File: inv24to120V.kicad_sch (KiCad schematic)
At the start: 133 parts, among them IC1 FSAM50SM60A, J1 Conn_02x13_Odd_Even_MountingP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, J10 Screw_Terminal_01x01, J11 Screw_Terminal_01x01, J12 Screw_Terminal_01x01, J2 Conn_02x13_Odd_Even_MountingP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, J3 Screw_Terminal_01x01, J4 Conn_02x05_Odd_Even_MountingP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, J5 Screw_Terminal_01x02, J6 Screw_Terminal_01x03, J7 Screw_Terminal_01x03, J8 Screw_Terminal_01x03, J9 Screw_Terminal_01x02, K1 J0971CS5VDC.45, Q1 IRFZ44NPBF, Q2 IRFZ44NPBF, Q3 2SC1815, Q4 2SC1815, Q5 2SA1015, Q6 2SA1015, Q7 2SC1815, U1 ESP32-DEVKITC-32D, U10 PC817, U2 LM2576HVT-5, U3 ACS712ELCTR30AT, U4 ACS712ELCTR30AT, U5 LM2576HVT-5, U6 ISO7340CDW, U7 ISO7340CDW, U8 AMC1300BDWVR, U9 PC817

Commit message: start rout
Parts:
- removed J1, J2: Conn_02x13_Odd_Even_MountingPin, Connector_IDC:IDC-Header_2x13_P2.54mm_Vertical, symbol Connector_Generic_MountingPin:Conn_02x13_Odd_Even_MountingPin
- removed J10, J11, J12, J3: Screw_Terminal_01x01, TerminalBlock_Wuerth:Wuerth_REDCUBE-THR_WP-THRBU_74650073_THR, symbol Connector:Screw_Terminal_01x01
- C10, C11, C12, C24, C25, C26, C27, C28, C29, C30, C31, C33, C34, C5, C6, C7, C8, C9: footprint Capacitor_SMD:C_0805_2012Metric -> Capacitor_SMD:C_0805_2012Metric_Pad1.18x1.45mm_HandSolder
- C13, C14, C15: footprint Capacitor_SMD:C_0805_2012Metric -> Capacitor_SMD:C_1206_3216Metric_Pad1.33x1.80mm_HandSolder
- R10, R22, R23, R24, R25, R26, R27, R28, R29, R30, R31, R32, R33, R34, R35, R36, R37, R7, R8, R9: footprint Resistor_SMD:R_0805_2012Metric -> Resistor_SMD:R_0805_2012Metric_Pad1.20x1.40mm_HandSolder
- R40, R44: footprint Resistor_THT:R_Axial_DIN0207_L6.3mm_D2.5mm_P10.16mm_Horizontal -> Resistor_SMD:R_0805_2012Metric_Pad1.20x1.40mm_HandSolder
- U1: footprint inv24VLib:MODULE_ESP32-DEVKITC-32D -> Connector_PinSocket_2.54mm:PinSocket_2x20_P2.54mm_Vertical
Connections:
- net FAULT_IPM2 is gone; now on net FAULT_IPM: R44.2, U10.4
- net GNDPWR1 is gone; now on net GNDPWR: R19.1, U8.3 (INN), X1.12, X1.13
- net I_Uphase2 is gone; now on net I_Uphase: R7.1, R9.2
- net I_Vphase2 is gone; now on net I_Vphase: R10.2, R8.1
- net TEMPERATURE_IPM2 is gone; now on net TEMPERATURE_IPM: BX6.1, C34.2, R40.2
- net UH2 is gone; now on an unnamed net: R29.1
- net UL2 is gone; now on an unnamed net: R32.1
- net VH2 is gone; now on an unnamed net: R30.1
- net VL2 is gone; now on an unnamed net: R33.1
- net VTH_IPM2 is gone; now on net VTH_IPM: IC1.24 (VTH)
- net WH2 is gone; now on an unnamed net: R31.1
- net WL2 is gone; now on an unnamed net: R34.1
- net +3.3V: now also U1.1 (3V3), U1.3 (EN); no longer U1.J2-1 (3V3), U1.J2-2 (EN)
- net +5V: now also U1.37 (EXT_5V); no longer U1.J2-19 (EXT_5V)
- net ANALOG_CMD: now also U1.11 (IO35); no longer U1.J2-6 (IO35)
- net DIGITAL_CMD: now also U1.16 (IO19); no longer U1.J3-8 (IO19)
- net FAULT_IPM: now also U1.4 (IO23); no longer U1.J3-2 (IO23)
- net GND: now also U1.14 (GND2), U1.2 (GND3), U1.27 (GND1); no longer U1.J2-14 (GND1), U1.J3-1 (GND3), U1.J3-7 (GND2)
- net GNDPWR: now also IC1.16 (COM(H))
- net I2C_SCL: now also U1.6 (IO22); no longer U1.J3-3 (IO22)
- net I2C_SDA: now also U1.12 (IO21); no longer U1.J3-6 (IO21)
- net I_Uphase: now also U1.5 (SENSOR_VP); no longer U1.J2-3 (SENSOR_VP)
- net I_Vphase: now also U1.7 (SENSOR_VN); no longer U1.J2-4 (SENSOR_VN)
- net PWM0_H: now also U1.29 (IO13); no longer U1.J2-15 (IO13)
- net PWM0_L: now also U1.25 (IO12); no longer U1.J2-13 (IO12)
- net PWM1_H: now also U1.23 (IO14); no longer U1.J2-12 (IO14)
- net PWM1_L: now also U1.21 (IO27); no longer U1.J2-11 (IO27)
- net PWM2_H: now also U1.19 (IO26); no longer U1.J2-10 (IO26)
- net PWM2_L: now also U1.17 (IO25); no longer U1.J2-9 (IO25)
- net RELAY_TRIP: now also U1.18 (IO18); no longer U1.J3-9 (IO18)
- net SCI_RXD: now also U1.24 (IO16); no longer U1.J3-12 (IO16)
- net SCI_TXD: now also U1.22 (IO17); no longer U1.J3-11 (IO17)
- net TEMPERATURE_IPM: now also U1.13 (IO32); no longer U1.J2-7 (IO32)
- net VBUS: now also L4.1, R17.2
- net VDC_sensor: now also U1.9 (IO34); no longer U1.J2-5 (IO34)
- net 150V_OUT1 renamed 150V_OUT
- net UH1: no longer names the net of U6.14 (OUTA)
- net UL1: no longer names the net of U7.14 (OUTA)
- net VH1: no longer names the net of U6.13 (OUTB)
- net VL1: no longer names the net of U7.13 (OUTB)
- net VTH_IPM1 renamed VTH_IPM
- net WH1: no longer names the net of U6.12 (OUTC)
- net WL1: no longer names the net of U7.12 (OUTC)
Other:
- moved on the sheet: C22

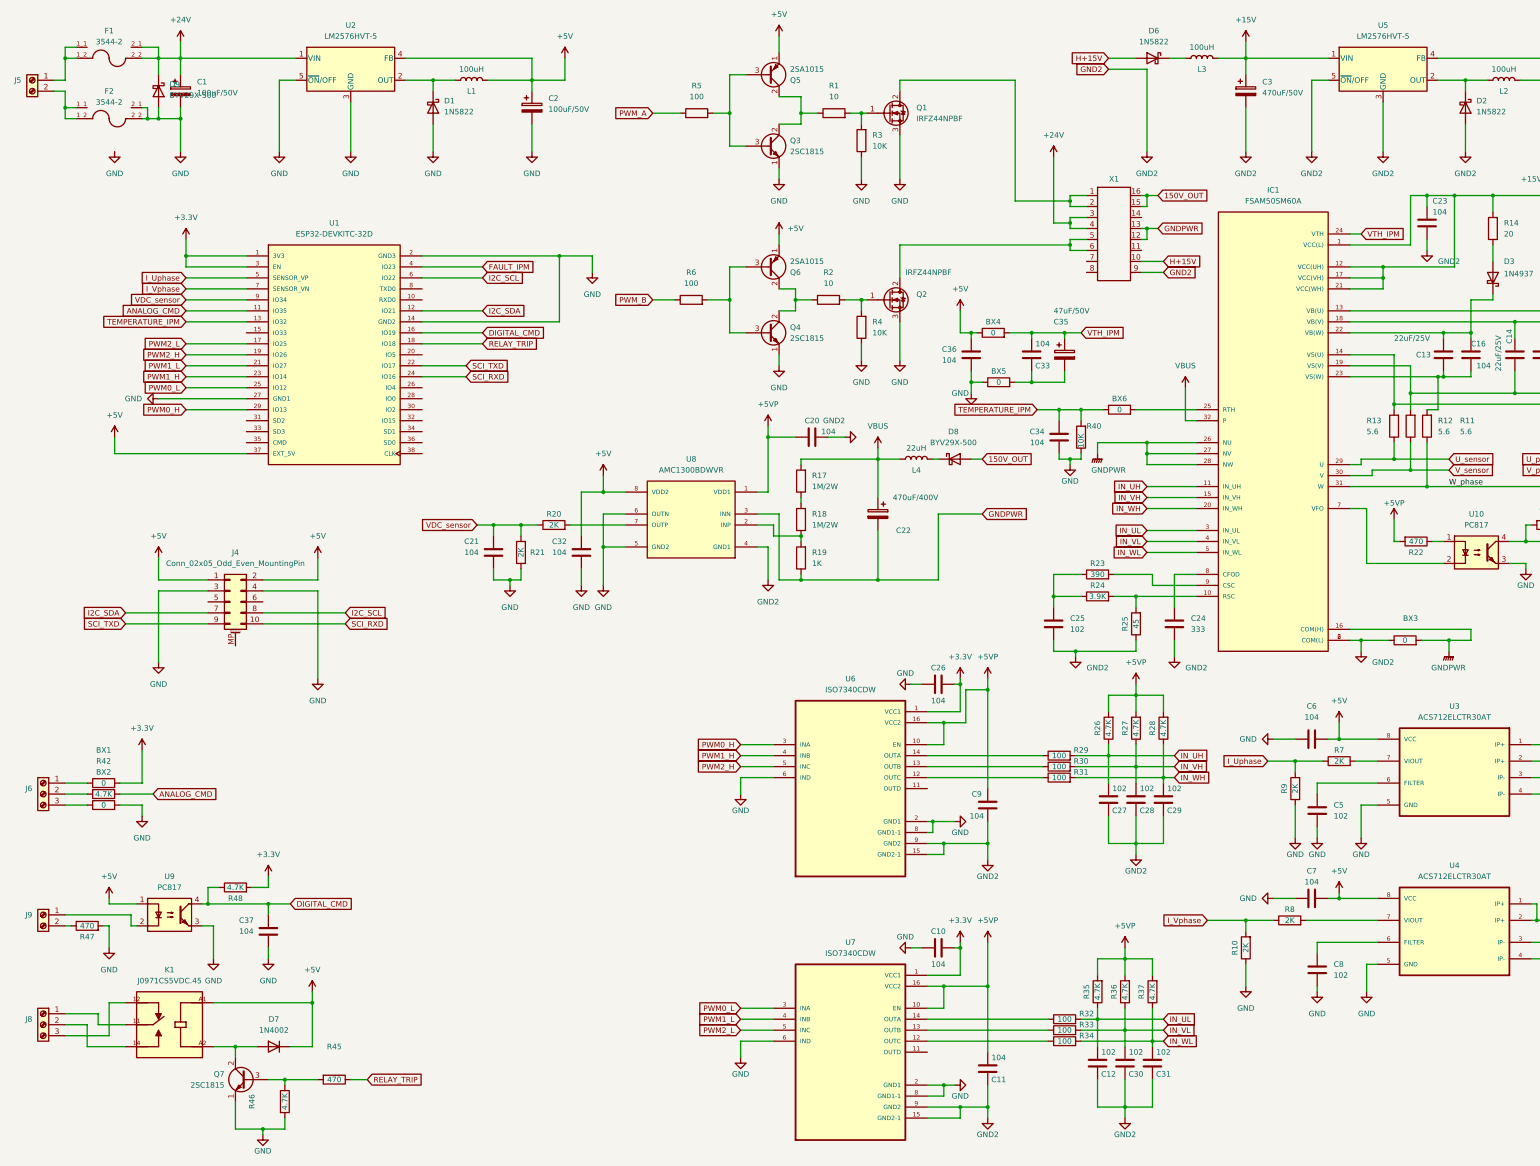
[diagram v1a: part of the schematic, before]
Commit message: remove aux addon connect
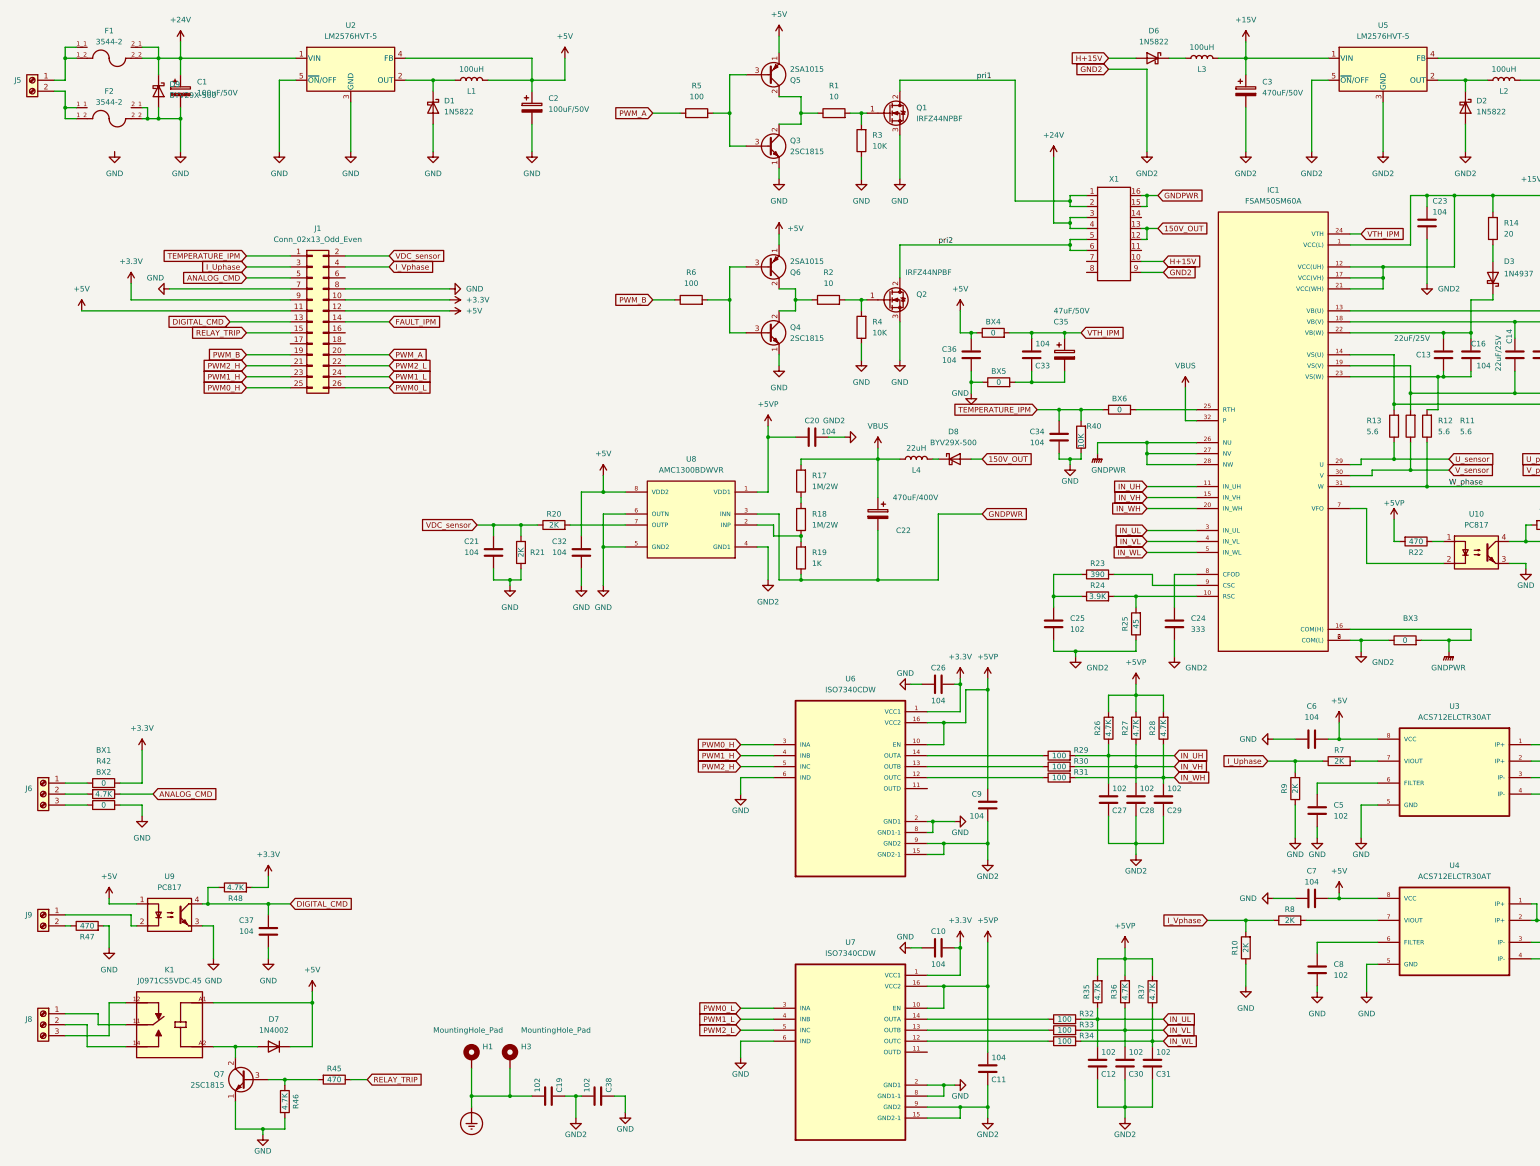
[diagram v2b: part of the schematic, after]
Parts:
- removed J4: Conn_02x05_Odd_Even_MountingPin, Connector_IDC:IDC-Header_2x05_P2.54mm_Vertical, symbol Connector_Generic_MountingPin:Conn_02x05_Odd_Even_MountingPin
- removed U1: ESP32-DEVKITC-32D, Connector_PinSocket_2.54mm:PinSocket_2x20_P2.54mm_Vertical, symbol esp32_worm:ESP32-DEVKITC-32D
- added C19, C38: 102, Capacitor_THT:C_Disc_D12.5mm_W5.0mm_P10.00mm, symbol Device:C
- added H1, H3: MountingHole_Pad, MountingHole:MountingHole_3.5mm_Pad_Via, symbol Mechanical:MountingHole_Pad
- added J1: Conn_02x13_Odd_Even, Connector_Hirose:Hirose_DF11-26DP-2DSA_2x13_P2.00mm_Vertical, symbol Connector_Generic:Conn_02x13_Odd_Even
- R11, R12, R13: footprint Resistor_THT:R_Axial_DIN0207_L6.3mm_D2.5mm_P10.16mm_Horizontal -> Resistor_THT:R_Axial_DIN0309_L9.0mm_D3.2mm_P15.24mm_Horizontal
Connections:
- net +3.3V: now also J1.10 (Pin_10), J1.9 (Pin_9)
- net +5V: now also J1.11 (Pin_11), J1.12 (Pin_12)
- net 150V_OUT: now also X1.12, X1.13; no longer X1.15, X1.16
- net ANALOG_CMD: now also J1.5 (Pin_5)
- net DIGITAL_CMD: now also J1.13 (Pin_13)
- net FAULT_IPM: now also J1.14 (Pin_14)
- net GND: now also C38.1, J1.7 (Pin_7), J1.8 (Pin_8)
- net GND2: now also C19.1, C38.2
- net GNDPWR: now also X1.15, X1.16; no longer X1.12, X1.13
- net I_Uphase: now also J1.3 (Pin_3)
- net I_Vphase: now also J1.4 (Pin_4)
- net PWM0_H: now also J1.25 (Pin_25)
- net PWM0_L: now also J1.26 (Pin_26)
- net PWM1_H: now also J1.23 (Pin_23)
- net PWM1_L: now also J1.24 (Pin_24)
- net PWM2_H: now also J1.21 (Pin_21)
- net PWM2_L: now also J1.22 (Pin_22)
- net PWM_A: now also J1.20 (Pin_20)
- net PWM_B: now also J1.19 (Pin_19)
- net RELAY_TRIP: now also J1.15 (Pin_15)
- net TEMPERATURE_IPM: now also J1.1 (Pin_1)
- net VDC_sensor: now also J1.2 (Pin_2)
- net pri2: now reaches Q2.2 (D), X1.5, X1.6
- net pri1: now reaches Q1.2 (D), X1.1, X1.2
- new net Earth_Protective: C19.2, H1.1, H3.1

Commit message: route done
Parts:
- removed F2: 3544-2, inv24VLib:FUSE_3544-2, symbol 3544-2:3544-2
- added C39, C41, C42: 104, Capacitor_SMD:C_0805_2012Metric, symbol Device:C
- added C40: 100uF/50V, Capacitor_THT:CP_Radial_D8.0mm_P5.00mm, symbol Device:C_Polarized
- added C43, C44: 22uF/10V, Capacitor_SMD:C_1210_3225Metric_Pad1.33x2.70mm_HandSolder, symbol Device:C_Polarized
- added U11: LM1117MP-3.3, Package_TO_SOT_SMD:SOT-223-3_TabPin2, symbol Regulator_Linear:LM1117MP-3.3
- C35: value 47uF/50V -> 22uF/10V; footprint Capacitor_THT:CP_Radial_D8.0mm_P5.00mm -> Capacitor_SMD:C_1210_3225Metric_Pad1.33x2.70mm_HandSolder
- D1, D2, D6: footprint Diode_THT:D_DO-201AD_P15.24mm_Horizontal -> Diode_THT:D_DO-201AD_P3.81mm_Vertical_AnodeUp
- D7: footprint Diode_THT:D_DO-41_SOD81_P10.16mm_Horizontal -> Diode_THT:D_DO-201AD_P3.81mm_Vertical_AnodeUp
- Q3: value 2SC1815 -> 2SC1815_SOT32; footprint Package_TO_SOT_THT:TO-92_Inline -> Package_TO_SOT_SMD:SOT-23-3
- Q4: value 2SC1815 -> 2SC1815_SOT32; footprint Package_TO_SOT_THT:TO-92_Inline -> Package_TO_SOT_SMD:SOT-23-3; symbol Transistor_BJT:2SC1815 -> New_Library:2SC1815_SOT32
- Q5: value 2SA1015 -> 2SA1015_SOT32; footprint Package_TO_SOT_THT:TO-92_Inline -> Package_TO_SOT_SMD:SOT-23-3
- Q6: value 2SA1015 -> 2SA1015_SOT32; footprint Package_TO_SOT_THT:TO-92_Inline -> Package_TO_SOT_SMD:SOT-23-3; symbol Transistor_BJT:2SA1015 -> New_Library:2SA1015_SOT32
- Q7: footprint Package_TO_SOT_THT:TO-92_Inline -> Package_TO_SOT_SMD:SOT-23-3; symbol Transistor_BJT:2SC1815 -> New_Library:2SC1815_SOT32
- R1, R2, R3, R4, R42, R45, R46, R48, R5, R6: footprint Resistor_THT:R_Axial_DIN0207_L6.3mm_D2.5mm_P10.16mm_Horizontal -> Resistor_SMD:R_0805_2012Metric_Pad1.20x1.40mm_HandSolder
- R11, R12, R13: footprint Resistor_THT:R_Axial_DIN0309_L9.0mm_D3.2mm_P15.24mm_Horizontal -> Resistor_THT:R_Axial_DIN0309_L9.0mm_D3.2mm_P20.32mm_Horizontal
- R47: value 470 -> 2k; footprint Resistor_THT:R_Axial_DIN0207_L6.3mm_D2.5mm_P10.16mm_Horizontal -> Resistor_SMD:R_0805_2012Metric_Pad1.20x1.40mm_HandSolder
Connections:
- net +24V: now also R47.1
- net +3.3V: now also C40.1, C41.2, C43.1, U11.2 (VO); no longer BX1.2, J1.10 (Pin_10), J1.9 (Pin_9)
- net +5V: now also BX1.2, Q5.2 (E), Q6.2 (E), C42.2, C44.1, U11.3 (VI); no longer Q5.1 (E), Q6.1 (E), U9.1
- net ANALOG_CMD: now also C39.2
- net GND: now also J5.2 (Pin_2), J9.2 (Pin_2), Q3.2 (E), Q4.2 (E), Q7.2 (E), C39.1, C40.2, C41.1, C42.1, C43.2, C44.2, U11.1 (GND); no longer Q3.1 (E), Q4.1 (E), Q7.1 (E), R47.2
- net at R45.2, R46.1: now also Q7.1 (B); no longer Q7.3 (B)
- net at D7.2 (A), K1.A2: now also Q7.3 (C); no longer Q7.2 (C)
- net at Q4.3 (C), Q6.3 (C): now also R2.1; no longer R6.2
- net at Q3.3 (C), Q5.3 (C): now also R1.1; no longer R5.2
- new net: R47.2, U9.1
- new net: Q4.1 (B), Q6.1 (B), R6.2
- new net: Q3.1 (B), Q5.1 (B), R5.2
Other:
- moved on the sheet: C1, C2, D1, D9, F1, J1, J5, L1, R47, R5, U2
